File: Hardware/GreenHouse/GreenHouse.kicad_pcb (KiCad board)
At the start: 2 copper layers, 132.6 x 92.7 mm, 25 parts, among them J1 12 V IN, J2 SENSORES TEMP, J3 DRIVER NEMA DERECHO, J4 DRIVER NEMA IZQUIERDO, J5 SEÑAL DESCANSO MOTOR, J6 FIN CARRERA, J7 FIN CARRERA VCC 5V, J8 SEÑAL MOTORES, U1 Ard_Pro_mini

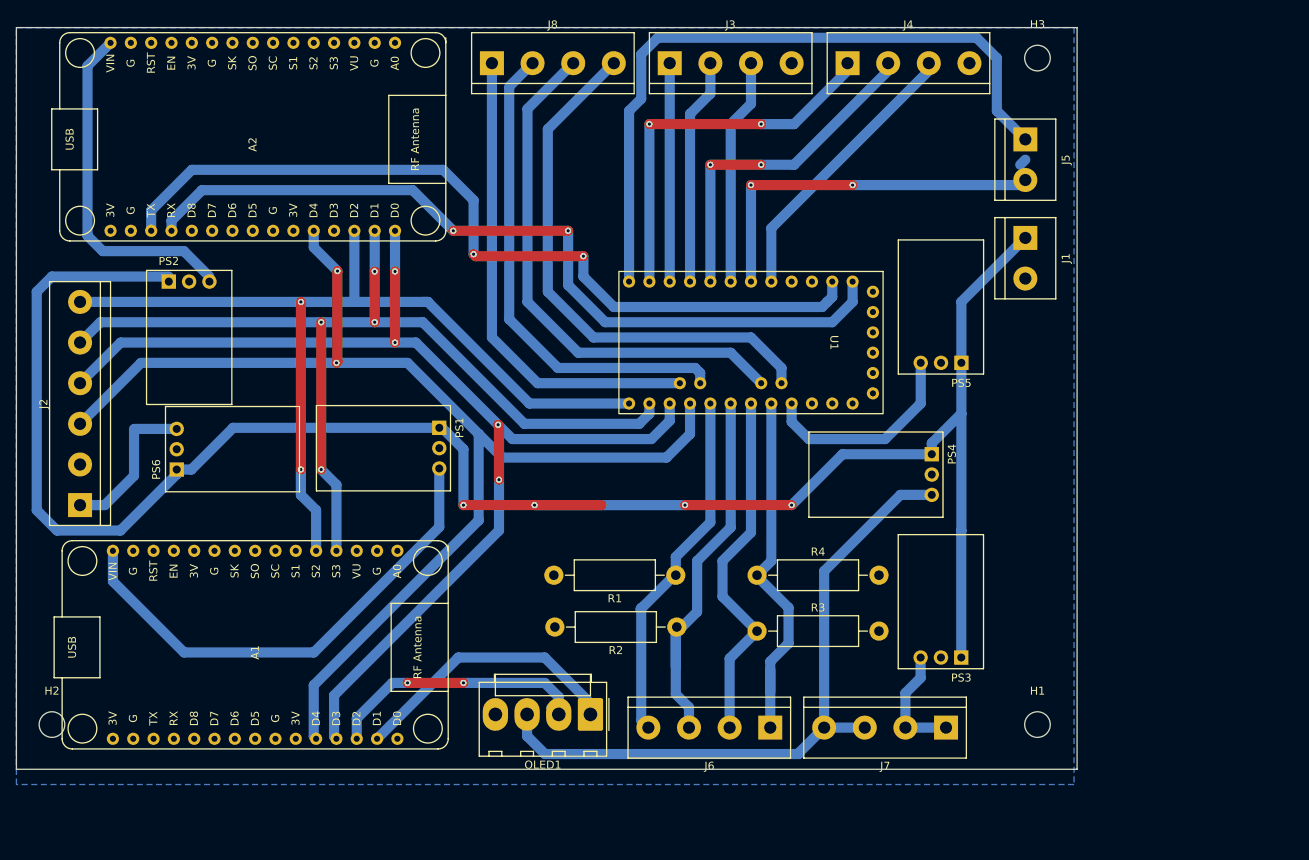
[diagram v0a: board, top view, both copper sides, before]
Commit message: fix: reduce the board size & re trace some parts.
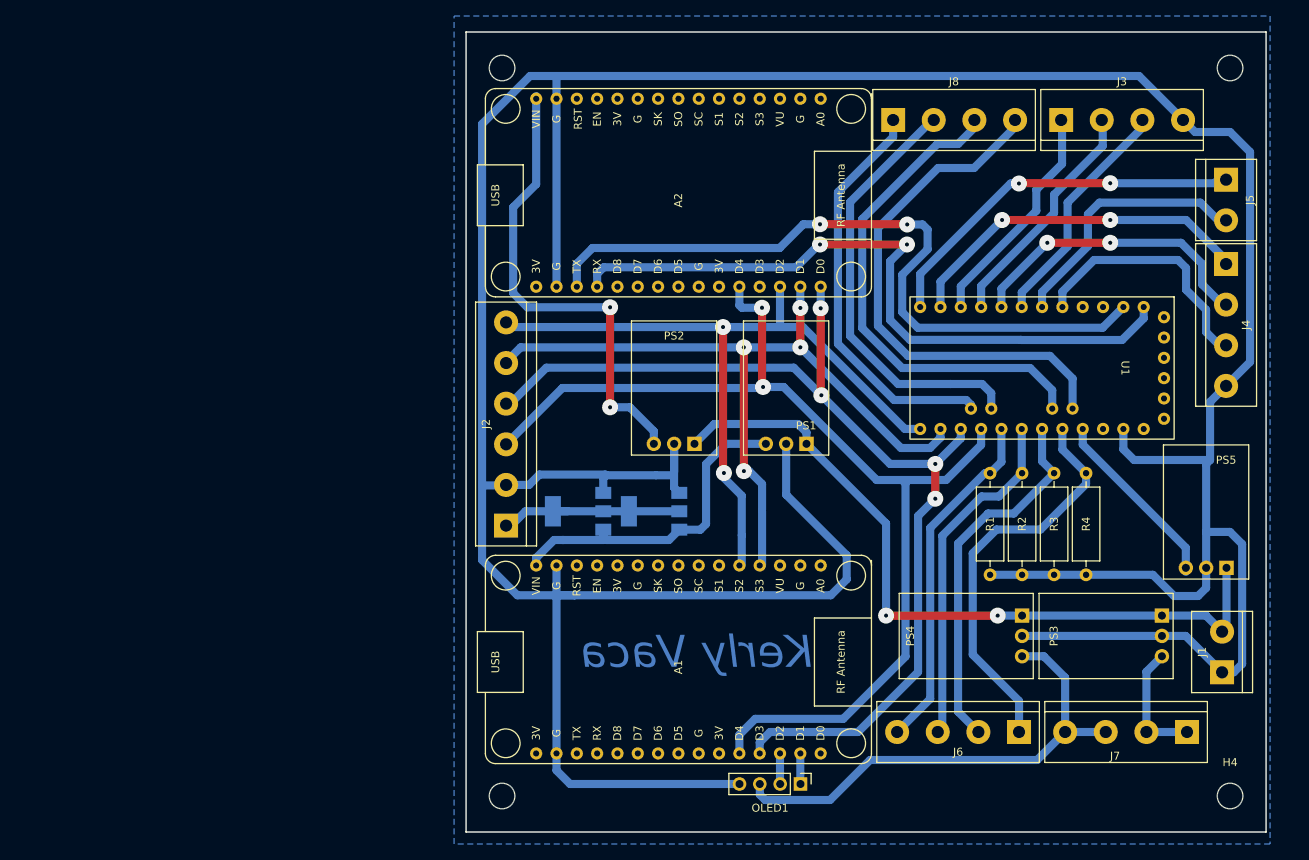
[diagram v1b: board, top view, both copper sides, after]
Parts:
- removed PS6: POLOLU 3V STEP UP/DOWN, Converter_DCDC:Converter_DCDC_Murata_OKI-78SR_Horizontal
- added H4: MountingHole, MountingHole:MountingHole_3.2mm_M3, F.Cu at (186.0, 140.5)
- added U2: AMS1117-3.3, Package_TO_SOT_SMD:SOT-223-3_TabPin2, B.Cu at (104.5, 104.9)
- added U3: AMS1117-3.3, Package_TO_SOT_SMD:SOT-223-3_TabPin2, B.Cu at (114.0, 104.9)
- OLED1: value SDA SCL VCC GND -> GND VCC SDA SCL; footprint Connector_Molex:Molex_KK-396_A-41791-0004_1x04_P3.96mm_Vertical -> Connector_PinHeader_2.54mm:PinHeader_1x04_P2.54mm_Vertical
- R1, R2, R3, R4: footprint Resistor_THT:R_Axial_DIN0411_L9.9mm_D3.6mm_P15.24mm_Horizontal -> Resistor_THT:R_Axial_DIN0309_L9.0mm_D3.2mm_P12.70mm_Horizontal
- moved H1 105.9 mm to (95.0, 49.5)
- moved PS2 68.8 mm to (119.0, 96.5), turned to 180 degrees
- moved J1 59.6 mm to (185.0, 125.0), turned to 90 degrees
- moved H2 57.0 mm to (95.0, 140.5)
- moved A2 53.7 mm to (115.8, 65.4)
- moved J4 53.6 mm to (185.5, 74.0), turned to -90 degrees
- moved J2 53.3 mm to (95.5, 106.7)
- moved A1 52.9 mm to (115.8, 123.8)
- moved J8 50.6 mm to (143.9, 56.0)
- moved J3 49.4 mm to (164.9, 56.0)
- moved R2 47.3 mm to (160.0, 100.2), turned to -90 degrees
- moved PS1 45.9 mm to (133.1, 96.5), turned to 180 degrees
- moved R4 43.1 mm to (168.0, 100.2), turned to -90 degrees
- moved R3 42.0 mm to (164.0, 100.2), turned to -90 degrees
- moved PS5 41.9 mm to (185.6, 112.0)
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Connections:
- net /5V_DISPLAY renamed /5V4
- net Net-(A1-Pad15) renamed /5V1
- net Net-(A2-Pad15) renamed /5V2
- net Net-(J7-Pad1) renamed /5V3
- net Net-(PS5-Pad3) renamed /5V5
- A1 pad 17: unconnected-(A1-Pad17) -> GND
- A2 pad 17: unconnected-(A2-Pad17) -> GND
- J1 pad 1: +12V -> GND
- J1 pad 2: GND -> +12V
- J3 pad 4: /DE - GND -> GND
- U1 pad 33: GND -> unconnected-(U1-Pad33)
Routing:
- net GND: track 0.00 -> 489.5 mm
- net +12V: track 244.7 -> 93.5 mm, vias 4 -> 2
- net /SEÑAL DESC MOT DER: track 87.0 -> 46.3 mm, vias 0 -> 2
- net Net-(A1-Pad29): track 34.6 -> 3.85 mm
- net Net-(A1-Pad28): track 33.2 -> 3.85 mm, vias 2 -> 0
- net /5V4: track 84.3 -> 61.7 mm
- net /SENSOR 3: track 120.1 -> 97.6 mm
- net /SENSOR 4: track 115.4 -> 93.2 mm
- net /5V1: track 62.1 -> 42.5 mm
- net /SENSOR 1: track 153.9 -> 135.6 mm
- net /5V2: track 42.7 -> 59.5 mm, vias 0 -> 2
- net Net-(A2-Pad19): track 102.4 -> 87.1 mm
- net Net-(A2-Pad18): track 104.7 -> 89.9 mm
- net /SEÑAL DESC MOT IZ: track 46.6 -> 31.8 mm, vias 2 -> 0
- net /SENSOR 2: track 145.8 -> 131.8 mm
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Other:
- board size 132.6 x 92.7 mm -> 100 x 100 mm
- board text added: "Kerly Vaca"

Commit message: docs: add Boom in Html
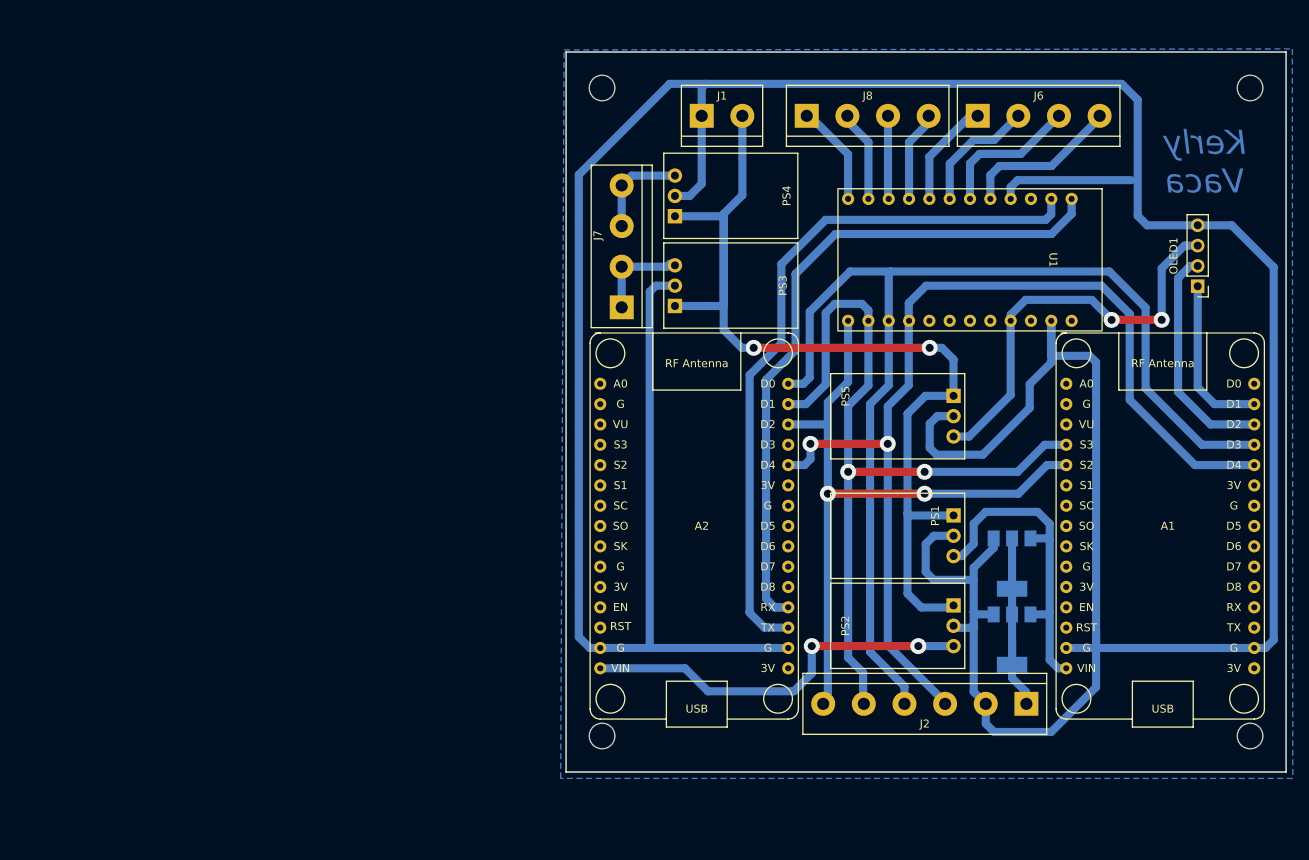
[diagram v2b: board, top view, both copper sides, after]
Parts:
- removed J3: DRIVER NEMA DERECHO, TerminalBlock:TerminalBlock_bornier-4_P5.08mm
- removed J4: DRIVER NEMA IZQUIERDO, TerminalBlock:TerminalBlock_bornier-4_P5.08mm
- removed J5: SEÑAL DESCANSO MOTOR, TerminalBlock:TerminalBlock_bornier-2_P5.08mm
- removed R1, R2, R3, R4: 220, Resistor_THT:R_Axial_DIN0309_L9.0mm_D3.2mm_P12.70mm_Horizontal
- J6: value FIN CARRERA -> SEÑAL MODULO RELE M2
- J8: value SEÑAL MOTORES -> SEÑAL MODULO RELE M1
- moved J1 95.2 mm to (120.0, 55.5), turned to 0 degrees
- moved H2 93.8 mm to (188.5, 133.0), turned to 90 degrees
- moved H4 88.5 mm to (188.5, 52.0), turned to 90 degrees
- moved J7 88.4 mm to (110.0, 79.4), turned to 90 degrees
- moved H1 84.4 mm to (107.5, 133.0), turned to 90 degrees
- moved OLED1 79.6 mm to (182.0, 76.8), turned to 180 degrees
- moved H3 78.5 mm to (107.5, 52.0), turned to 90 degrees
- moved J6 77.2 mm to (154.5, 55.5), turned to 0 degrees
- moved PS3 72.1 mm to (116.6, 79.2), turned to 90 degrees
- moved J2 68.8 mm to (160.5, 129.0), turned to 180 degrees
- moved PS4 66.1 mm to (116.6, 68.0), turned to 90 degrees
- moved A1 63.8 mm to (177.6, 108.0), turned to 0 degrees
- moved U2 56.6 mm to (158.8, 120.9), turned to -90 degrees
- moved U3 45.2 mm to (158.8, 111.4), turned to -90 degrees
- moved A2 42.8 mm to (119.3, 108.0), turned to 0 degrees
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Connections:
- J6 pad 1: /RETORNO VCC FC4 -> Net-(J6-Pad1)
- J6 pad 2: /RETORNO VCC FC3 -> Net-(J6-Pad2)
- J6 pad 3: /RETORNO VCC FC2 -> Net-(J6-Pad3)
- J6 pad 4: /RETORNO VCC FC1 -> Net-(J6-Pad4)
- OLED1 pad 3: /5V4 -> /5V5
- U1 pad 10: /RETORNO VCC FC4 -> unconnected-(U1-Pad10)
- U1 pad 11: /SEÑAL DESC MOT IZ -> Net-(J6-Pad3)
- U1 pad 12: /RETORNO VCC FC3 -> unconnected-(U1-Pad12)
- U1 pad 13: /DE - CW- -> Net-(J6-Pad2)
- U1 pad 14: /RETORNO VCC FC2 -> unconnected-(U1-Pad14)
- U1 pad 15: /IZ - PWM CLK+ -> Net-(J6-Pad1)
- U1 pad 16: /RETORNO VCC FC1 -> unconnected-(U1-Pad16)
- U1 pad 17: /DE - PWM CLK+ -> Net-(J8-Pad4)
- U1 pad 19: /DE - EN+ -> Net-(J8-Pad3)
- U1 pad 21: /IZ - EN+ -> Net-(J8-Pad2)
- U1 pad 23: /SEÑAL DESC MOT DER -> Net-(J8-Pad1)
- U1 pad 9: /IZ - CW- -> Net-(J6-Pad4)
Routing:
- net Net-(J8-Pad4): track 66.3 -> 11.4 mm
- net Net-(J8-Pad3): track 62.6 -> 10.3 mm
- net /RETORNO VCC FC4: track 50.6 -> 0.00 mm
- net /5V4: track 61.7 -> 11.6 mm
- net /RETORNO VCC FC3: track 46.4 -> 0.00 mm
- net /SEÑAL DESC MOT DER: track 46.3 -> 0.00 mm, vias 2 -> 0
- net /IZ - EN+: track 44.4 -> 0.00 mm, vias 2 -> 0
- net /RETORNO VCC FC1: track 44.4 -> 0.00 mm
- net /RETORNO VCC FC2: track 43.5 -> 0.00 mm
- net Net-(J8-Pad2): track 54.1 -> 11.3 mm
- net Net-(J8-Pad1): track 51.1 -> 12.4 mm
- net /IZ - PWM CLK+: track 36.5 -> 0.00 mm, vias 2 -> 0
- net +12V: track 93.5 -> 128.7 mm
- net /SEÑAL DESC MOT IZ: track 31.8 -> 0.00 mm
- net /IZ - CW-: track 31.7 -> 0.00 mm
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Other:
- board size 100 x 100 mm -> 90 x 90 mm
